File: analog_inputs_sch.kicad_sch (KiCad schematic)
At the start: 51 parts, among them J1 Conn_Coaxial, J2 Conn_Coaxial, J7 Conn_Coaxial, K10 G2RL-2, K8 G2RL-2, K9 G2RL-2, U1 OPA656U, U15 OPA2277, U18 OPA2277, U8 OPA656U

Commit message: Save work on simplifying the desing
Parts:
- removed unit 1 of U15
- removed unit 1 of U18
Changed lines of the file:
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@@
 	)
 	(junction
-		(at 245.11 44.45)
-		(diameter 0)
-		(color 0 0 0 0)
-	)
-	(junction
 		(at 149.86 121.92)
 		(diameter 0)
@@
 	)
 	(junction
-		(at 245.11 118.11)
-		(diameter 0)
-		(color 0 0 0 0)
-	)
-	(junction
 		(at 86.36 64.77)
 		(diameter 0)
@@
 	)
 	(symbol
-		(lib_id "Amplifier_Operational:OPA2277")
-		(at 252.73 41.91 0)
-		(mirror x)
-		(unit 1)
-		(exclude_from_sim no)
-		(in_bom yes)
-		(on_board yes)
-		(dnp no)
-		(property "Reference" "U15"
-			(at 254.762 35.306 0)
-			(effects
-				(font
-					(size 1.27 1.27)
-				)
-			)
-		)
-		(property "Value" "OPA2277"
-			(at 255.524 32.258 0)
-			(effects
-				(font
-					(size 1.27 1.27)
-				)
-			)
-		)
-		(property "Footprint" ""
-			(at 252.73 41.91 0)
-			(effects
-				(font
-					(size 1.27 1.27)
-				)
-				(hide yes)
-			)
-		)
-		(property "Datasheet" "https://www.ti.com/lit/ds/symlink/opa2277.pdf"
-			(at 252.73 41.91 0)
-			(effects
-				(font
-					(size 1.27 1.27)
-				)
-				(hide yes)
-			)
-		)
-		(property "Description" "Dual High Precision Operational Amplifiers, DIP-8/SOIC-8"
-			(at 252.73 41.91 0)
-			(effects
-				(font
-					(size 1.27 1.27)
-				)
-				(hide yes)
-			)
-		)
-		(pin "4"
-		)
-		(pin "8"
-		)
-		(pin "6"
-		)
-		(pin "5"
-		)
-		(pin "2"
-		)
-		(pin "1"
-		)
-		(pin "3"
-		)
-		(pin "7"
-		)
-		(instances
-			(project ""
-				(path "/553deb7b-4100-40fe-99d2-0c7b4b56aad2/c6e88111-c18e-4095-b1d8-9b944099aec3"
-					(reference "U15")
-					(unit 1)
-				)
-			)
-		)
-	)
-	(symbol
 		(lib_id "Device:R")
 		(at 231.14 44.45 90)
@@
 					(unit 1)
 				)
-			)
-		)
-	)
-	(symbol
-		(lib_id "Amplifier_Operational:OPA2277")
-		(at 252.73 115.57 0)
-		(mirror x)
-		(unit 1)
-		(exclude_from_sim no)
-		(in_bom yes)
-		(on_board yes)
-		(dnp no)
-		(property "Reference" "U18"
-			(at 254.762 109.22 0)
-			(effects
-				(font
-					(size 1.27 1.27)
-				)
-			)
-		)
-		(property "Value" "OPA2277"
-			(at 255.27 106.426 0)
-			(effects
-				(font
-					(size 1.27 1.27)
-				)
-			)
-		)
-		(property "Footprint" ""
-			(at 252.73 115.57 0)
-			(effects
-				(font
-					(size 1.27 1.27)
-				)
-				(hide yes)
-			)
-		)
-		(property "Datasheet" "https://www.ti.com/lit/ds/symlink/opa2277.pdf"
-			(at 252.73 115.57 0)
-			(effects
-				(font
-					(size 1.27 1.27)
-				)
-				(hide yes)
-			)
-		)
-		(property "Description" "Dual High Precision Operational Amplifiers, DIP-8/SOIC-8"
-			(at 252.73 115.57 0)
-			(effects
-				(font
-					(size 1.27 1.27)
-				)
-				(hide yes)
-			)
-		)
-		(pin "4"
-		)
-		(pin "7"
-		)
-		(pin "6"
-		)
-		(pin "1"
-		)
-		(pin "3"
-		)
-		(pin "5"
-		)
-		(pin "8"
-		)
-		(pin "2"
-		)
-		(instances
-			(project ""
-				(path "/553deb7b-4100-40fe-99d2-0c7b4b56aad2/c6e88111-c18e-4095-b1d8-9b944099aec3"
-					(reference "U18")
-					(unit 1)
-				)

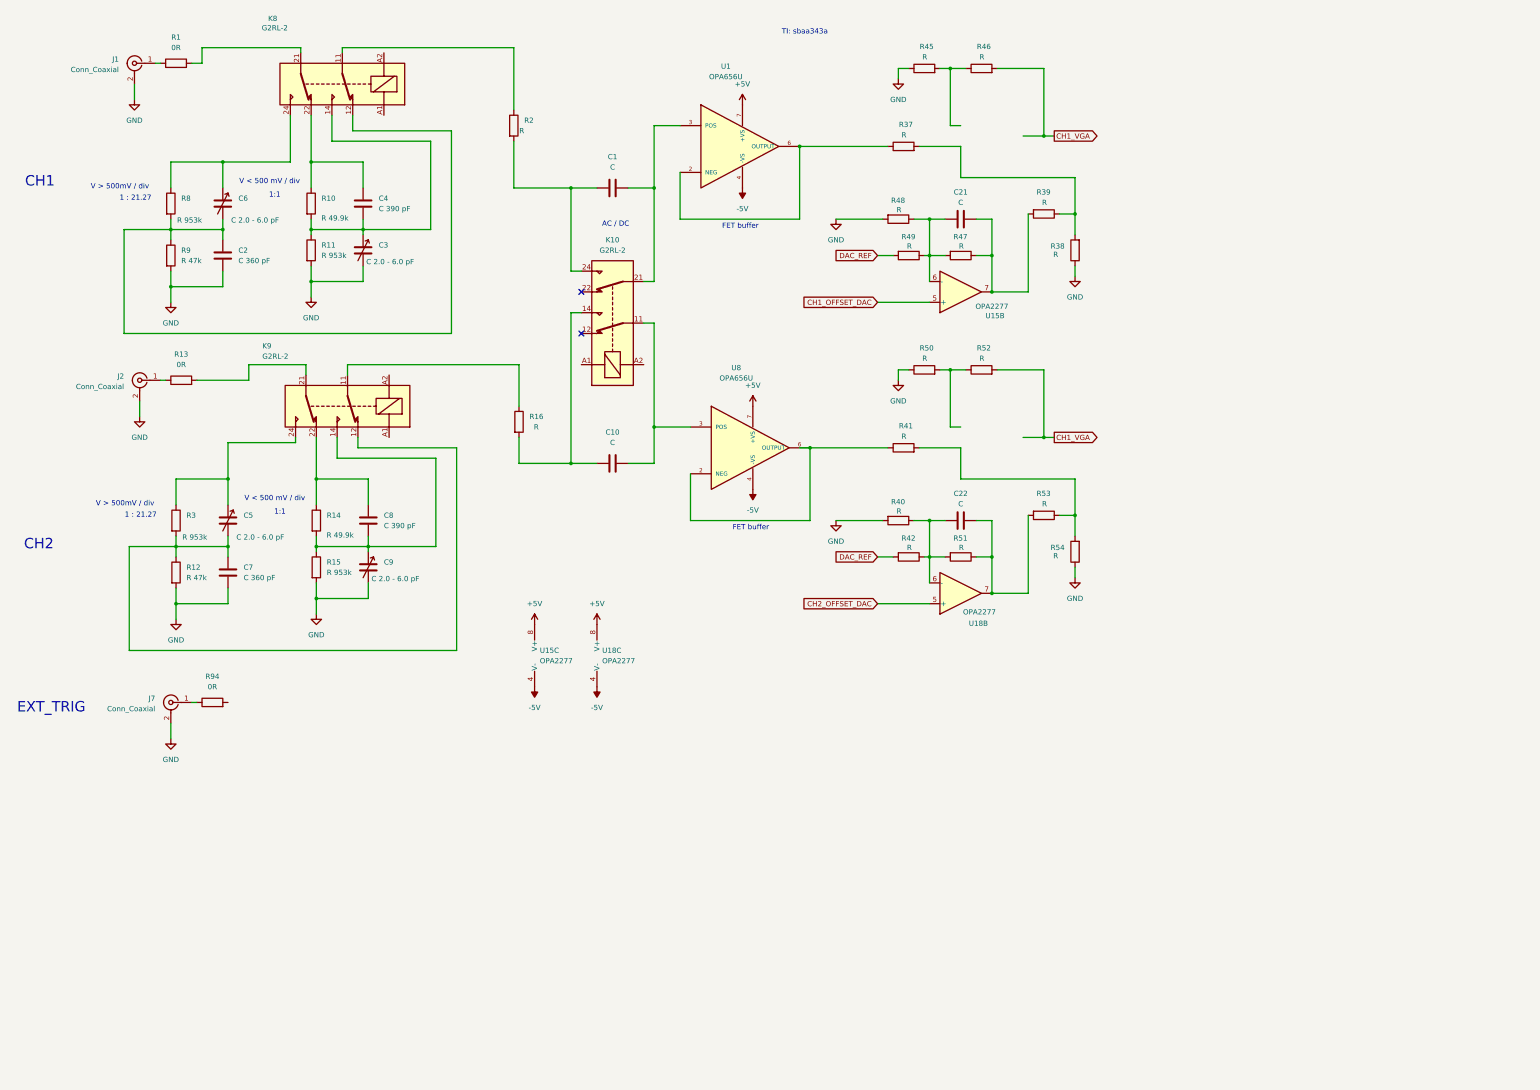
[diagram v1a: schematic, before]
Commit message: Simplifying the design
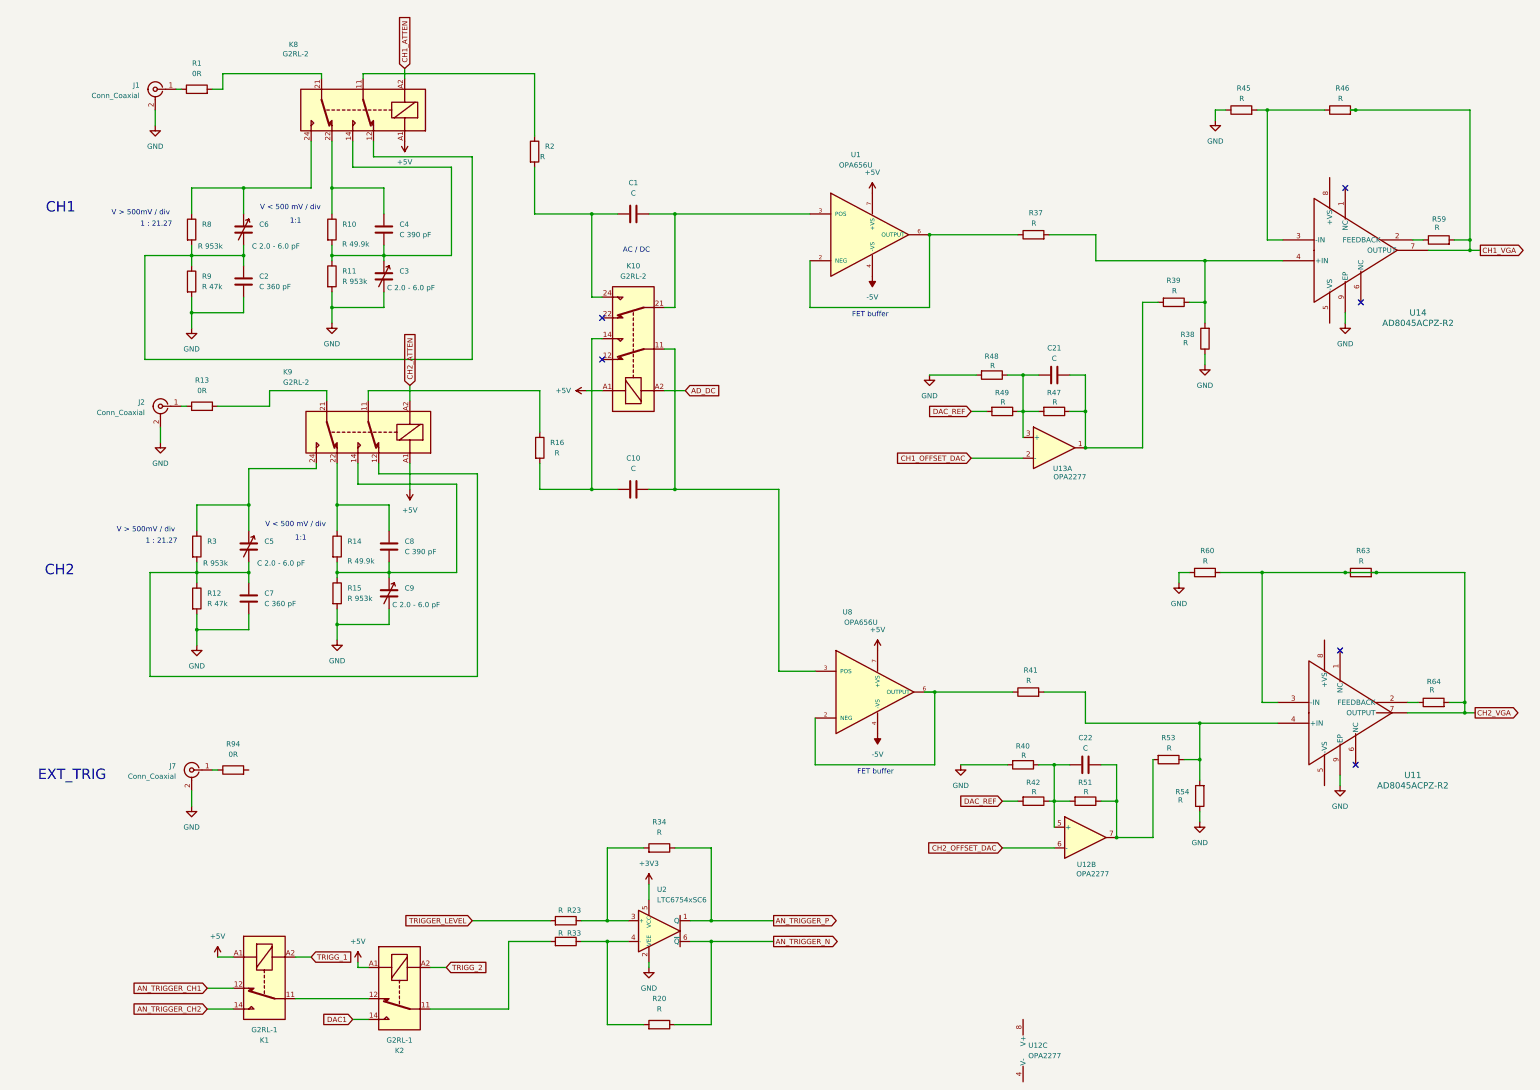
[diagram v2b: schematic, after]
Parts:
- removed R50, R52: R, symbol Device:R
- removed U15, U18: OPA2277, symbol Amplifier_Operational:OPA2277
- added K1, K2: G2RL-1, Relay_THT:Relay_SPDT_Omron_G2RL-1, symbol Relay:G2RL-1
- added R20, R23, R33, R34, R59, R60, R63, R64: R, symbol Device:R
- added U11, U14: AD8045ACPZ-R2, CP_8_2_ADI, symbol 2025-07-01_23-44-10:AD8045ACPZ-R2
- added U12, U13: OPA2277, symbol Amplifier_Operational:OPA2277
- added U2: LTC6754xSC6, Package_TO_SOT_SMD:SOT-363_SC-70-6, symbol Comparator:LTC6754xSC6
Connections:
- net +5V: now also K10.A1, K8.A1, K9.A1, K1.A1, K2.A1
- net CH1_OFFSET_DAC: now also U13.2 (-)
- net CH1_VGA: now also R59.2, U14.7 (OUTPUT)
- net CH2_OFFSET_DAC: now also U12.6 (-)
- net GND: now also R60.1, U11.9 (EP), U14.9 (EP), U2.2 (VEE)
- net at R41.2, R53.1, R54.2: now also U11.4 (+IN)
- net at R37.2, R38.2, R39.1: now also U14.4 (+IN)
- net at R45.2, R46.1: now also U14.3 (-IN)
- net at C22.2, R51.1, R53.2: now also U12.7
- net at C21.1, R47.2, R48.1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: now also U13.3 (+)
- net at C21.2, R39.2, R47.1: now also U13.1
- net at C22.1, R40.1, R42.1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: now also U12.5 (+)
- net CH1_ATTEN: now reaches K8.A2
- net CH2_ATTEN: now reaches K9.A2
- net AD_DC: now reaches K10.A2
- new net: R59.1, U14.2 (FEEDBACK)
- new net: R23.1, R34.2, U2.3 (+)
- new net: R20.2, R33.1, U2.4 (-)
- new net: K2.11, R33.2
- new net: R64.1, U11.2 (FEEDBACK)
- new net: K1.11, K2.12
- new net +3V3: U2.5 (VCC)
- new net AN_TRIGGER_CH1: K1.12
- new net AN_TRIGGER_CH2: K1.14
- new net AN_TRIGGER_N: R20.1, U2.6 (~{Q})
- new net AN_TRIGGER_P: R34.1, U2.1 (Q)
- new net CH2_VGA: R60.2, R63.1, R63.2, R64.2, U11.3 (-IN), U11.7 (OUTPUT)
- new net DAC1: K2.14
- new net TRIGGER_LEVEL: R23.2
- new net TRIGG_1: K1.A2
- new net TRIGG_2: K2.A2
- no-connect marks 2 -> 6
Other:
- note removed: "TI: sbaa343a"
- moved on the sheet: C1, C10, C2, C21, C22, C3, C4, C5, C6, C7, C8, C9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

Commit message: Gain on diff amp 0.2
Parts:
- R1, R13, R94: value 0R -> 33R
- R16: value R -> 33 R
- R2, R37, R41: value R -> 33R
- R20, R34: value R -> DNP
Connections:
- net DAC1: now also R23.2; no longer K2.14
- net TRIGGER_LEVEL: now also K2.14, R94.2; no longer R23.2
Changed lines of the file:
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@@
 	(wire
 		(pts
-			(xy 45.72 96.52) (xy 125.73 96.52)
+			(xy 45.72 97.79) (xy 125.73 97.79)
 		)
 		(stroke
@@
 	(wire
 		(pts
-			(xy 45.72 71.12) (xy 45.72 96.52)
+			(xy 45.72 71.12) (xy 45.72 97.79)
 		)
 		(stroke
@@
 	(wire
 		(pts
-			(xy 96.52 257.81) (xy 100.33 257.81)
+			(xy 99.06 257.81) (xy 100.33 257.81)
 		)
 		(stroke
@@
 	(wire
 		(pts
-			(xy 125.73 46.99) (xy 125.73 96.52)
+			(xy 125.73 46.99) (xy 125.73 97.79)
 		)
 		(stroke
@@
 	(wire
 		(pts
-			(xy 110.49 102.87) (xy 110.49 106.68)
+			(xy 110.49 95.25) (xy 110.49 106.68)
 		)
 		(stroke
@@
 	(global_label "CH2_ATTEN"
 		(shape input)
-		(at 110.49 102.87 90)
+		(at 110.49 95.25 90)
 		(fields_autoplaced yes)
 		(effects
@@
 		)
 		(property "Intersheetrefs" "${INTERSHEET_REFS}"
-			(at 110.49 89.6039 90)
+			(at 110.49 81.9839 90)
 			(effects
 				(font
@@
 		)
 	)
-	(global_label "DAC1"
+	(global_label "TRIGGER_LEVEL"
 		(shape input)
-		(at 96.52 257.81 180)
+		(at 71.12 196.85 0)
 		(fields_autoplaced yes)
 		(effects
@@
 				(size 1.27 1.27)
 			)
-			(justify right)
+			(justify left)
 		)
 		(property "Intersheetrefs" "${INTERSHEET_REFS}"
-			(at 88.6967 257.81 0)
+			(at 88.317 196.85 0)
 			(effects
 				(font
 					(size 1.27 1.27)
 				)
-				(justify right)
+				(justify left)
 				(hide yes)
 			)
@@
 		)
 	)
-	(global_label "TRIGGER_LEVEL"
-		(shape input)
-		(at 125.73 233.68 180)
-		(fields_autoplaced yes)
-		(effects
-			(font
-				(size 1.27 1.27)
-			)
-			(justify right)
-		)
-		(property "Intersheetrefs" "${INTERSHEET_REFS}"
-			(at 108.533 233.68 0)
-			(effects
-				(font
-					(size 1.27 1.27)
-				)
-				(justify right)
-				(hide yes)
-			)
-		)
-	)
 	(global_label "CH2_VGA"
 		(shape output)
@@
 		)
 	)
+	(global_label "DAC1"
+		(shape input)
+		(at 125.73 233.68 180)
+		(fields_autoplaced yes)
+		(effects
+			(font
+				(size 1.27 1.27)
+			)
+			(justify right)
+		)
+		(property "Intersheetrefs" "${INTERSHEET_REFS}"
+			(at 117.9067 233.68 0)
+			(effects
+				(font
+					(size 1.27 1.27)
+				)
+				(justify right)
+				(hide yes)
+			)
+		)
+	)
+	(global_label "TRIGGER_LEVEL"
+		(shape input)
+		(at 99.06 257.81 180)
+		(fields_autoplaced yes)
+		(effects
+			(font
+				(size 1.27 1.27)
+			)
+			(justify right)
+		)
+		(property "Intersheetrefs" "${INTERSHEET_REFS}"
+			(at 81.863 257.81 0)
+			(effects
+				(font
+					(size 1.27 1.27)
+				)
+				(justify right)
+				(hide yes)
+			)
+		)
+	)
 	(symbol
 		(lib_name "AD8045ACPZ-R2_2")
@@
 			)
 		)
-		(property "Value" "R"
+		(property "Value" "33R"
 			(at 261.112 175.006 90)
 			(effects
@@
 			)
 		)
-		(property "Value" "R"
+		(property "Value" "DNP"
 			(at 171.45 212.09 90)
 			(effects
@@
 			)
 		)
-		(property "Value" "R"
-			(at 147.066 119.38 0)
+		(property "Value" "33 R"
+			(at 147.828 119.38 0)
 			(effects
 				(font
@@
 			)
 		)
-		(property "Value" "R"
+		(property "Value" "DNP"
 			(at 171.45 255.27 90)
 			(effects
@@
 			)
 		)
-		(property "Value" "R"
-			(at 262.382 63.246 90)
+		(property "Value" "33R"
+			(at 261.366 63.246 90)
 			(effects
 				(font
@@
 			)
 		)
-		(property "Value" "0R"
+		(property "Value" "33R"
 			(at 59.69 104.14 90)
 			(effects
@@
 			)
 		)
-		(property "Value" "R"
-			(at 143.51 46.9899 0)
+		(property "Value" "33R"
+			(at 147.066 46.99 0)
 			(effects
 				(font
@@
 			)
 		)
-		(property "Value" "0R"
+		(property "Value" "33R"
 			(at 67.31 193.04 90)
 			(effects
@@
 			)
 		)
-		(property "Value" "0R"
+		(property "Value" "33R"
 			(at 58.42 26.67 90)
 			(effects

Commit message: Mostly finished schematics, without decoupling and power
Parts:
- added C56, C57, C58, C59: DNP, symbol Device:C
- added TP1, TP10, TP11, TP12, TP13, TP14, TP15, TP16, TP17, TP18, TP2, TP3, TP4, TP5, TP6, TP7, TP8, TP9: TestPoint, Connector_PinHeader_2.54mm:PinHeader_1x01_P2.54mm_Vertical, symbol Connector:TestPoint
- C1, C10: value C -> 22nF
- C21, C22: value C -> 22pF
- C6: value C 2.0 - 6.0 pF -> C 2.0 - 10.0 pF
- R1, R10, R11, R12, R13, R14, R15, R16, R2, R20, R23, R3, R33, R34, R37, R41, R8, R94: footprint (none) -> Resistor_SMD:R_1206_3216Metric
- R38, R39, R45, R46, R53, R54, R60, R63: value R -> 10k; footprint (none) -> Resistor_SMD:R_1206_3216Metric
- R40, R47, R48, R51: value R -> 16k; footprint (none) -> Resistor_SMD:R_1206_3216Metric
- R42, R49: value R -> 8k; footprint (none) -> Resistor_SMD:R_1206_3216Metric
- R59, R64: value R -> 0R; footprint (none) -> Resistor_SMD:R_1206_3216Metric
- R9: value R 47k -> R 22.2k; footprint (none) -> Resistor_SMD:R_1206_3216Metric
- U11, U14: footprint CP_8_2_ADI -> footprints:CP_8_2_ADI
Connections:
- net +5V: now also U11.8 (+VS), U12.8 (V+), U14.8 (+VS)
- net -5V: now also U11.5 (-VS), U12.4 (V-)
- net AN_TRIGGER_N: now also TP18.1
- net AN_TRIGGER_P: now also TP17.1
- net CH1_OFFSET_DAC: now also TP12.1
- net CH1_VGA: now also TP6.1
- net CH2_OFFSET_DAC: now also TP10.1
- net CH2_VGA: now also TP14.1; no longer R60.2, R63.1, U11.3 (-IN)
- net DAC1: now also TP16.1
- net GND: now also C57.2, C58.2
- net at R37.2, R38.2, R39.1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: now also TP4.1
- net at R41.2, R53.1, R54.2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: now also TP13.1
- net at C5.2, C7.1, K9.12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: now also C59.2
- net at K9.11, R16.1: now also TP8.1
- net at C3.1, C4.2, K8.14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: now also C57.1
- net at C22.2, R51.1, R53.2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: now also TP11.1
- net at K2.11, R33.2: now also TP15.1
- net at C8.2, C9.1, K9.14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: now also C58.1
- net at C10.2, K10.11, U8.3 (POS): now also TP9.1
- net at C2.1, C6.2, K8.12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: now also C56.2
- net at K9.21, R13.2: now also TP7.1
- net at C21.2, R39.2, R47.1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: now also TP5.1
- net at C1.2, K10.21, U1.3 (POS): now also TP3.1
- net at K8.11, R2.1: now also TP2.1
- net at C6.1, K8.24, R8.1: now also C56.1
- net at K8.21, R1.2: now also TP1.1
- net at C5.1, K9.24, R3.1: now also C59.1
- new net: R60.2, R63.1, U11.3 (-IN)
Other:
- note added: "sbaa343a"
- note added: "~ 1 : 44"
- moved on the sheet: C3, C5, C6, C9, R11, R15, R3, R45, R8, U12C

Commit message: Finished schematic?
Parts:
- added C100, C103, C106, C109, C112, C115, C118, C121, C124, C97: 100nF, symbol Device:C
- added C101, C104, C107, C110, C113, C116, C119, C122, C125, C127, C98: 1uF, symbol Device:C
- added C102, C105, C108, C111, C114, C117, C120, C123, C126, C99: 10uF, symbol Device:C
- added L35, L37, L39, L41, L43, L45, L47, L49, L51, L53: LCBB-601, symbol Device:L
- added L36, L38, L40, L42, L44, L46, L48, L50, L52, L54: 0.68uH, 0.8Ohm, symbol Device:L
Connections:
- net +3V3: now also C127.2
- net +5V: now also L36.1, L38.1, L40.1, L48.1, L52.1; no longer U1.7 (+VS), U11.8 (+VS), U12.8 (V+), U14.8 (+VS), U8.7 (+VS)
- net -5V: now also L42.1, L44.1, L46.1, L50.1, L54.1; no longer U1.4 (-VS), U11.5 (-VS), U12.4 (V-), U8.4 (-VS)
- net GND: now also C100.2, C101.1, C102.1, C103.2, C104.1, C105.1, C106.2, C107.1, C108.1, C109.2, C110.1, C111.1, C112.2, C113.1, C114.1, C115.2, C116.1, C117.1, C118.2, C119.1, C120.1, C121.2, C122.1, C123.1, C124.2, C125.1, C126.1, C127.1, C97.2, C98.1, C99.1
- net at U14.5 (-VS): now also C112.1, C113.2, C114.2, L45.2
- new net: C100.1, C101.2, C102.2, L37.2, U14.8 (+VS)
- new net: L43.1, L44.2
- new net: C115.1, C116.2, C117.2, L47.2, U1.7 (+VS)
- new net: L45.1, L46.2
- new net: L51.1, L52.2
- new net: C121.1, C122.2, C123.2, L51.2, U8.7 (+VS)
- new net: L37.1, L38.2
- new net: L47.1, L48.2
- new net: C97.1, C98.2, C99.2, L35.2, U11.8 (+VS)
- new net: C124.1, C125.2, C126.2, L53.2, U8.4 (-VS)
- new net: C103.1, C104.2, C105.2, L39.2, U12.8 (V+)
- new net: L35.1, L36.2
- new net: C106.1, C107.2, C108.2, L41.2, U12.4 (V-)
- new net: C109.1, C110.2, C111.2, L43.2, U11.5 (-VS)
- new net: L49.1, L50.2
- new net: C118.1, C119.2, C120.2, L49.2, U1.4 (-VS)
- new net: L39.1, L40.2
- new net: L41.1, L42.2
- new net: L53.1, L54.2
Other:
- note removed: "FET buffer"
- moved on the sheet: C1, C10, C2, C21, C22, C3, C4, C5, C56, C57, C58, C59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

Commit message: Save work after calculating AF
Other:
- note removed: "1 : 21.27"
- moved on the sheet: R46
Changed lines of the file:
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@@
 	(generator_version "9.0")
 	(paper "A2")
-	(text "V < 500 mV / div"
-		(exclude_from_sim no)
-		(at 99.06 155.956 0)
-		(effects
-			(font
-				(size 1.27 1.27)
-			)
-		)
-	)
 	(text "CH2"
 		(exclude_from_sim no)
@@
 		)
 	)
-	(text "1:1"
-		(exclude_from_sim no)
-		(at 156.464 168.91 0)
-		(effects
-			(font
-				(size 1.27 1.27)
-			)
-		)
-	)
 	(text "V < 500 mV / div"
 		(exclude_from_sim no)
-		(at 155.194 165.608 0)
+		(at 156.21 157.988 0)
 		(effects
 			(font
@@
 	(text "V > 500mV / div"
 		(exclude_from_sim no)
-		(at 52.07 151.384 0)
+		(at 97.282 147.828 0)
 		(effects
 			(font
@@
 		)
 	)
+	(text "1:1"
+		(exclude_from_sim no)
+		(at 157.48 161.29 0)
+		(effects
+			(font
+				(size 1.27 1.27)
+			)
+		)
+	)
 	(text "V > 500mV / div"
 		(exclude_from_sim no)
@@
 		)
 	)
-	(text "1 : 21.27"
+	(text "~ 1 : 44\n"
 		(exclude_from_sim no)
-		(at 55.88 154.178 0)
+		(at 100.076 79.502 0)
 		(effects
 			(font
@@
 	(text "~ 1 : 44\n"
 		(exclude_from_sim no)
-		(at 100.076 79.502 0)
+		(at 101.092 150.622 0)
 		(effects
 			(font
@@
 	(wire
 		(pts
-			(xy 472.44 111.76) (xy 500.38 111.76)
+			(xy 481.33 111.76) (xy 500.38 111.76)
 		)
 		(stroke
@@
 	(wire
 		(pts
-			(xy 450.85 111.76) (xy 464.82 111.76)
+			(xy 450.85 111.76) (xy 473.71 111.76)
 		)
 		(stroke
@@
 	(symbol
 		(lib_id "Device:R")
-		(at 468.63 111.76 90)
+		(at 477.52 111.76 90)
 		(unit 1)
 		(exclude_from_sim no)
@@
 		(dnp no)
 		(property "Reference" "R46"
-			(at 470.916 106.426 90)
+			(at 479.806 106.426 90)
 			(effects
 				(font
@@
 		)
 		(property "Value" "10k"
-			(at 468.122 108.966 90)
+			(at 477.012 108.966 90)
 			(effects
 				(font
@@
 		)
 		(property "Footprint" "Resistor_SMD:R_1206_3216Metric"
-			(at 468.63 113.538 90)
+			(at 477.52 113.538 90)
 			(effects
 				(font
@@
 		)
 		(property "Datasheet" "~"
-			(at 468.63 111.76 0)
+			(at 477.52 111.76 0)
 			(effects
 				(font
@@
 		)
 		(property "Description" "Resistor"
-			(at 468.63 111.76 0)
+			(at 477.52 111.76 0)
 			(effects
 				(font
